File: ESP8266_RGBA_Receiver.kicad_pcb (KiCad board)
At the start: 2 copper layers, 24.3 x 28.8 mm, 20 parts, among them J1 RGBAConnector, P1 ISP, Q1 PMV16XNR, Q2 PMV16XNR, Q3 PMV16XNR, Q4 PMV16XNR, SW1 SW_Push, U1 MCP1702-3302_SOT223, U2 ESP-07

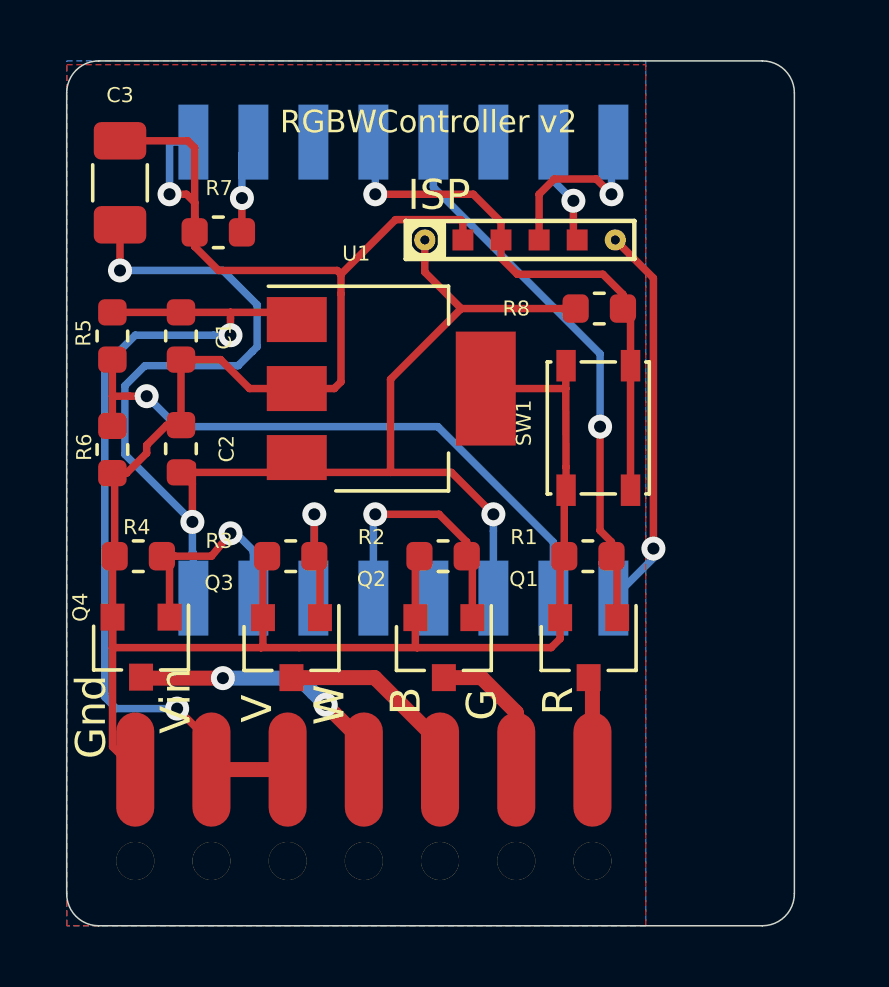
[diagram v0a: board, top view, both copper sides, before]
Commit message: v3 as ordered on JLC PCB: ------------------------- - Replaced LED connector with Molex straddle mounted on the PCB - Moved button from GPIO0 to GPIO5 - Enlarged holes for powerinput
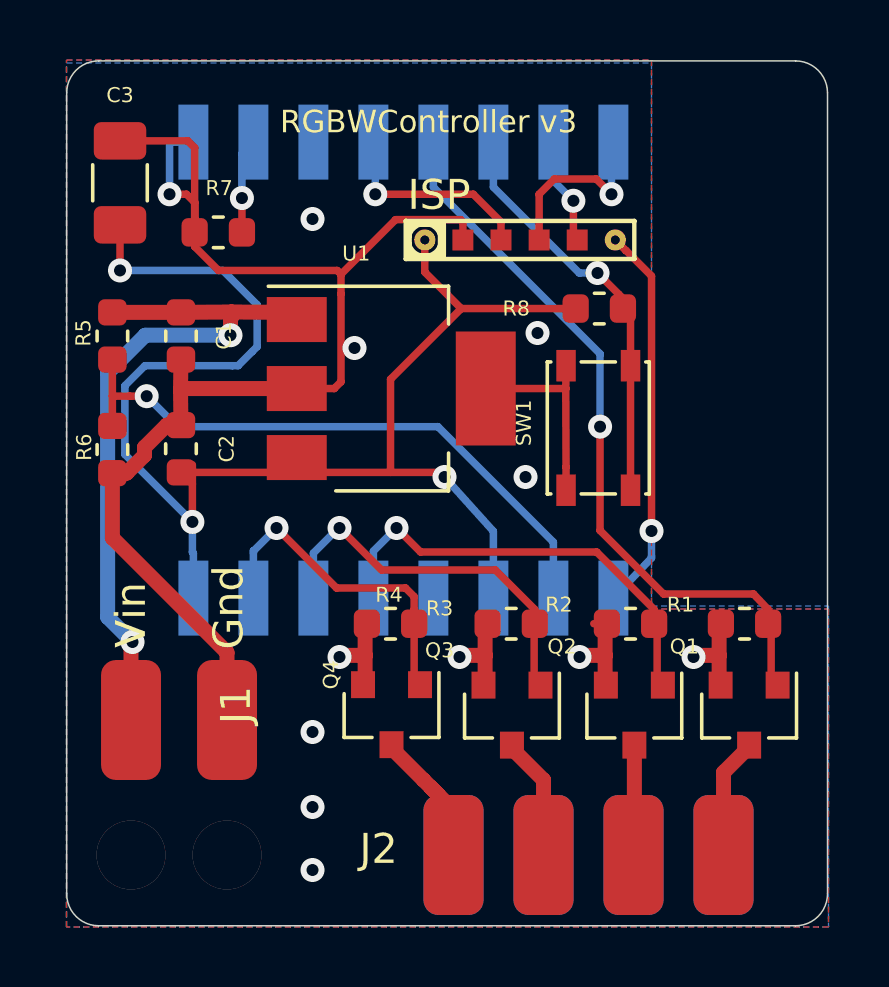
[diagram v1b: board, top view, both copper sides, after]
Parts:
- added J2: Conn_02x04_Counter_Clockwise, footprint:MolexMicroFit3.0_2x8_StradleMount, F.Cu at (91.0, 78.5)
- J1: value RGBAConnector -> Vin_Solderpad; footprint footprint:7Wire_Solder -> footprint:2Wire_Solder_large
- R6: value 820R -> 560R
- moved J1 15.5 mm to (80.2, 71.5)
- moved R4 8.70 mm to (88.9, 68.3)
- moved Q4 8.65 mm to (88.9, 71.3)
- moved Q3 7.69 mm to (92.9, 71.3)
- moved R3 7.69 mm to (92.9, 68.3)
- moved Q2 6.74 mm to (97.0, 71.3)
- moved R2 6.64 mm to (96.9, 68.3)
- moved Q1 5.80 mm to (100.9, 71.3)
- moved R1 5.69 mm to (100.7, 68.3)
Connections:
- J1 pad 1: /LED_R -> GND
- J1 pad 2: /LED_G -> VBUS
- R8 pad 1: /GPIO0 -> /GPIO5
- SW1 pad 1: /GPIO0 -> /GPIO5
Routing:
- net GND: track 80.6 -> 65.0 mm, vias 1 -> 12
- net /GPIO5: track 0.00 -> 13.9 mm, vias 0 -> 1
- net /GPIO0: track 18.7 -> 6.94 mm
- net VBUS: track 30.7 -> 23.9 mm
- net /GPIO12: track 6.33 -> 13.0 mm
- net /GPIO4: track 18.4 -> 24.3 mm
- net /GPIO14: track 8.85 -> 14.7 mm
- net /GPIO13: track 7.36 -> 12.1 mm
- net /LED_A: track 9.22 -> 4.89 mm, vias 2 -> 0
- net /LED_B: track 6.74 -> 4.10 mm
- net /LED_G: track 4.80 -> 3.67 mm
- net /LED_R: track 3.12 -> 4.02 mm
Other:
- board size 24.3 x 28.8 mm -> 25.4 x 28.8 mm
- board text added: "RGBWController v3"
- board text removed: "RGBWController v2"
